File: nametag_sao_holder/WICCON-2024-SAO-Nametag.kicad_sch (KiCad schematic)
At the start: 20 parts, among them J1 Conn_02x03_Odd_Even, J2 Conn_02x03_Odd_Even, J3 Conn_02x03_Odd_Even, J4 Conn_02x03_Odd_Even, J5 Conn_02x03_Odd_Even, J6 Conn_02x03_Odd_Even, J7 Conn_02x03_Odd_Even, J8 Conn_02x03_Odd_Even, SW1 ON/OFF, U1 QX2303L33E

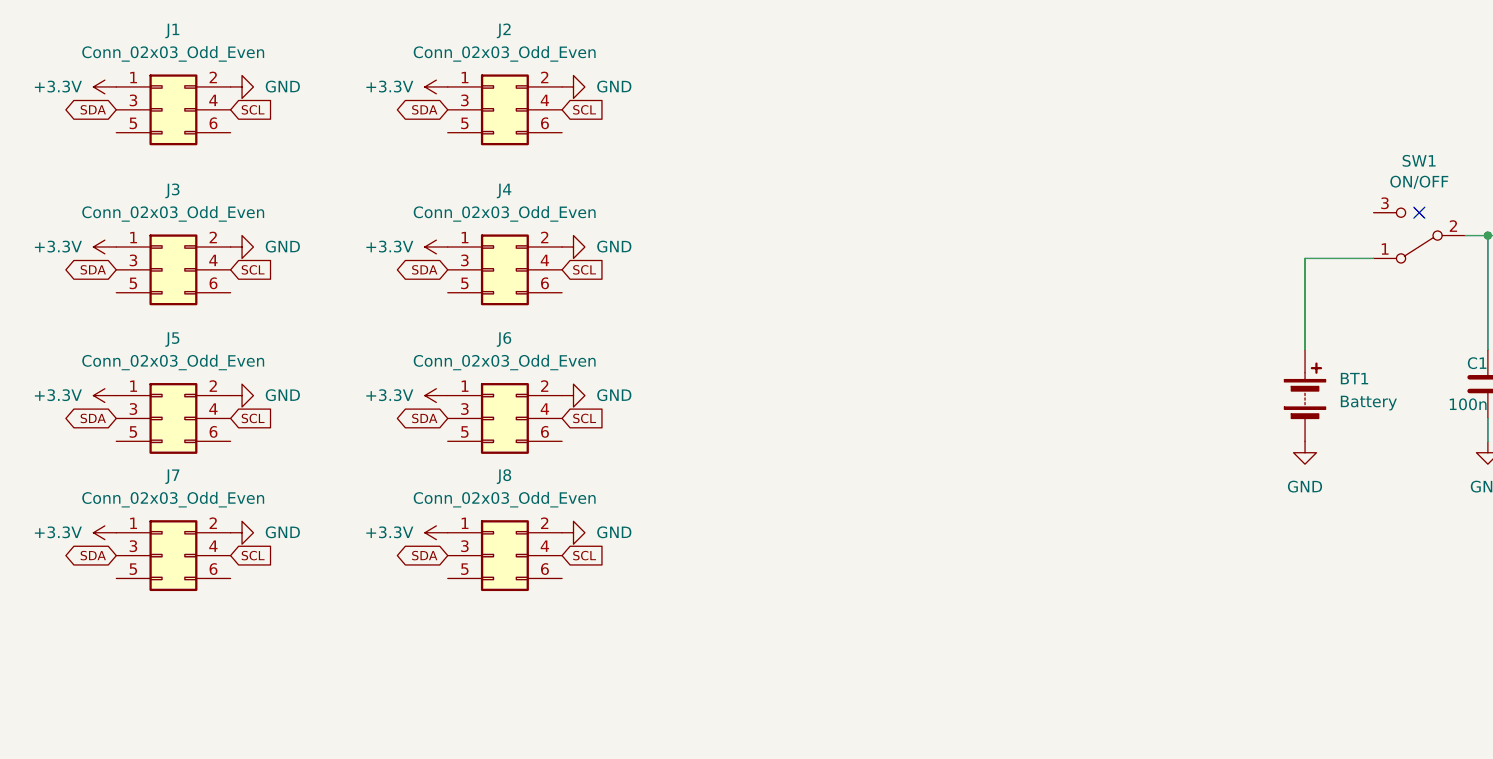
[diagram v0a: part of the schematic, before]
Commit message: Apply some improvements based on review by Paul
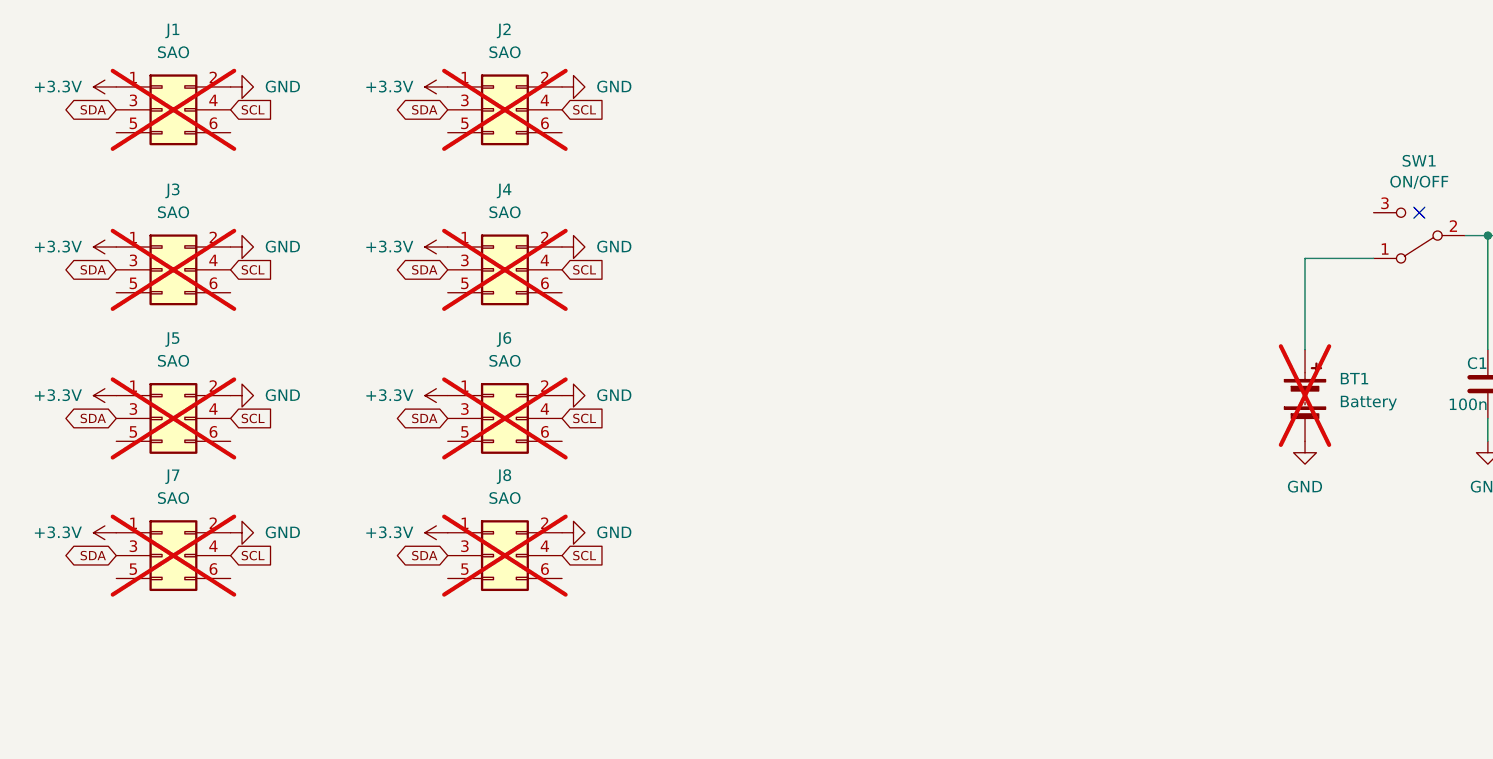
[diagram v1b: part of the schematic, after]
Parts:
- BT1: now not fitted; now left out of the parts list
- C1, C3: LCSC (none) -> C361203
- D1: LCSC (none) -> C5185907
- J1, J2, J3, J4, J5, J6, J7, J8: value Conn_02x03_Odd_Even -> SAO; now not fitted; now left out of the parts list
- SW1: LCSC (none) -> C319020
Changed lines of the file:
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@@
 			)
 		)
-		(property "Datasheet" "http://www.vishay.com/docs/88525/1n5817.pdf"
+		(property "Datasheet" "https://www.lcsc.com/product-detail/Schottky-Diodes_Slkor-SLKORMICRO-Elec-1N5819W_C5185907.html"
 			(at 222.25 44.45 0)
 			(effects
@@
 			)
 		)
+		(property "LCSC" "C5185907"
+			(at 222.25 44.45 0)
+			(effects
+				(font
+					(size 1.27 1.27)
+				)
+				(hide yes)
+			)
+		)
 		(pin "1"
 		)
@@
 			)
 		)
-		(property "Datasheet" ""
+		(property "Datasheet" "https://www.lcsc.com/product-detail/Power-Inductors_COILANK-INTERNATIONAL-ABG06A28M470_C253589.html"
 			(at 204.47 44.45 0)
 			(effects
@@
 			)
 		)
-		(property "Datasheet" "~"
+		(property "Datasheet" "https://www.lcsc.com/product-detail/Multilayer-Ceramic-Capacitors-MLCC-SMD-SMT_TDK-C1005X5R1E104KT000E_C361203.html"
 			(at 193.04 60.96 0)
 			(effects
@@
 		)
 		(property "Description" ""
+			(at 193.04 60.96 0)
+			(effects
+				(font
+					(size 1.27 1.27)
+				)
+				(hide yes)
+			)
+		)
+		(property "LCSC" "C361203"
 			(at 193.04 60.96 0)
 			(effects
@@
 			)
 		)
-		(property "Datasheet" "~"
+		(property "Datasheet" "https://www.lcsc.com/product-detail/Slide-Switches_XKB-Connection-SK-3296S-01-L1_C319020.html"
 			(at 185.42 44.45 0)
 			(effects
@@
 			)
 		)
+		(property "LCSC" "C319020"
+			(at 185.42 44.45 0)
+			(effects
+				(font
+					(size 1.27 1.27)
+				)
+				(hide yes)
+			)
+		)
 		(pin "1"
 		)
@@
 		(unit 1)
 		(exclude_from_sim no)
-		(in_bom yes)
-		(on_board yes)
-		(dnp no)
+		(in_bom no)
+		(on_board yes)
+		(dnp yes)
 		(fields_autoplaced yes)
 		(property "Reference" "J3"
@@
 			)
 		)
-		(property "Value" "Conn_02x03_Odd_Even"
+		(property "Value" "SAO"
 			(at 46.99 41.91 0)
 			(effects
@@
 		(unit 1)
 		(exclude_from_sim no)
-		(in_bom yes)
-		(on_board yes)
-		(dnp no)
+		(in_bom no)
+		(on_board yes)
+		(dnp yes)
 		(fields_autoplaced yes)
 		(property "Reference" "J7"
@@
 			)
 		)
-		(property "Value" "Conn_02x03_Odd_Even"
+		(property "Value" "SAO"
 			(at 46.99 73.66 0)
 			(effects
@@
 		(unit 1)
 		(exclude_from_sim no)
-		(in_bom yes)
-		(on_board yes)
-		(dnp no)
+		(in_bom no)
+		(on_board yes)
+		(dnp yes)
 		(fields_autoplaced yes)
 		(property "Reference" "J1"
@@
 			)
 		)
-		(property "Value" "Conn_02x03_Odd_Even"
+		(property "Value" "SAO"
 			(at 46.99 24.13 0)
 			(effects
@@
 			)
 		)
-		(property "Datasheet" "~"
+		(property "Datasheet" "https://www.lcsc.com/product-detail/Multilayer-Ceramic-Capacitors-MLCC-SMD-SMT_TDK-C1005X5R1E104KT000E_C361203.html"
 			(at 232.41 60.96 0)
 			(effects
@@
 			)
 		)
+		(property "LCSC" "C361203"
+			(at 232.41 60.96 0)
+			(effects
+				(font
+					(size 1.27 1.27)
+				)
+				(hide yes)
+			)
+		)
 		(pin "1"
 		)
@@
 		(unit 1)
 		(exclude_from_sim no)
-		(in_bom yes)
-		(on_board yes)
-		(dnp no)
+		(in_bom no)
+		(on_board yes)
+		(dnp yes)
 		(fields_autoplaced yes)
 		(property "Reference" "J5"
@@
 			)
 		)
-		(property "Value" "Conn_02x03_Odd_Even"
+		(property "Value" "SAO"
 			(at 46.99 58.42 0)
 			(effects
@@
 		(unit 1)
 		(exclude_from_sim no)
-		(in_bom yes)
-		(on_board yes)
-		(dnp no)
+		(in_bom no)
+		(on_board yes)
+		(dnp yes)
 		(fields_autoplaced yes)
 		(property "Reference" "J8"
@@
 			)
 		)
-		(property "Value" "Conn_02x03_Odd_Even"
+		(property "Value" "SAO"
 			(at 83.82 73.66 0)
 			(effects
@@
 		(unit 1)
 		(exclude_from_sim no)
-		(in_bom yes)
-		(on_board yes)
-		(dnp no)
+		(in_bom no)
+		(on_board yes)
+		(dnp yes)
 		(fields_autoplaced yes)
 		(property "Reference" "J4"
@@
 			)
 		)
-		(property "Value" "Conn_02x03_Odd_Even"
+		(property "Value" "SAO"
 			(at 83.82 41.91 0)
 			(effects
@@
 		(unit 1)
 		(exclude_from_sim no)
-		(in_bom yes)
-		(on_board yes)
-		(dnp no)
+		(in_bom no)
+		(on_board yes)
+		(dnp yes)
 		(fields_autoplaced yes)
 		(property "Reference" "J2"
@@
 			)
 		)
-		(property "Value" "Conn_02x03_Odd_Even"
+		(property "Value" "SAO"
 			(at 83.82 24.13 0)
 			(effects
@@
 		(unit 1)
 		(exclude_from_sim no)
-		(in_bom yes)
-		(on_board yes)
-		(dnp no)
+		(in_bom no)
+		(on_board yes)
+		(dnp yes)
 		(fields_autoplaced yes)
 		(property "Reference" "BT1"
@@
 		(unit 1)
 		(exclude_from_sim no)
-		(in_bom yes)
-		(on_board yes)
-		(dnp no)
+		(in_bom no)
+		(on_board yes)
+		(dnp yes)
 		(fields_autoplaced yes)
 		(property "Reference" "J6"
@@
 			)
 		)
-		(property "Value" "Conn_02x03_Odd_Even"
+		(property "Value" "SAO"
 			(at 83.82 58.42 0)
 			(effects

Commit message: Add missing production files
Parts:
- H1, H2: LCSC (none) -> -
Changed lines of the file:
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@@
+			)
+		)
+		(property "LCSC" "-"
+			(at 250.19 158.75 0)
+			(effects
+				(font
+					(size 1.27 1.27)
+				)
+				(hide yes)
 			)
 		)
@@
 			(at 250.19 153.67 0)
 			(effects
+				(font
+					(size 1.27 1.27)
+				)
+				(hide yes)
+			)
+		)
+		(property "LCSC" "-"
+			(at 250.19 153.67 0)
+			(effects

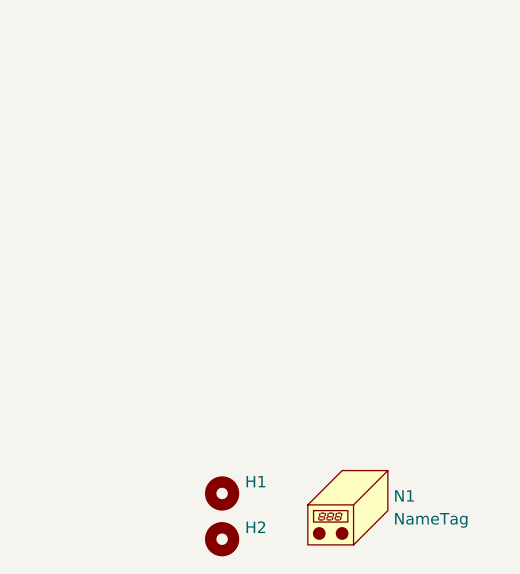
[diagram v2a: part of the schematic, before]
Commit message: Added text and art
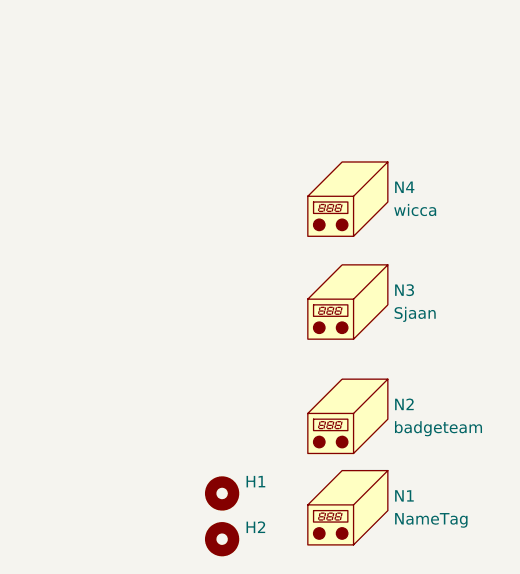
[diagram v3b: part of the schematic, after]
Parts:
- added N2: badgeteam, Library:stamp, symbol Mechanical:Housing
- added N3: Sjaan, Library:Chantal, symbol Mechanical:Housing
- added N4: wicca, Library:full_wicca_logo, symbol Mechanical:Housing
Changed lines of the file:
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@@
+	)
+	(symbol
+		(lib_id "Mechanical:Housing")
+		(at 265.43 132.08 0)
+		(unit 1)
+		(exclude_from_sim yes)
+		(in_bom no)
+		(on_board yes)
+		(dnp no)
+		(fields_autoplaced yes)
+		(property "Reference" "N3"
+			(at 269.24 131.1274 0)
+			(effects
+				(font
+					(size 1.27 1.27)
+				)
+				(justify left)
+			)
+		)
+		(property "Value" "Sjaan"
+			(at 269.24 133.6674 0)
+			(effects
+				(font
+					(size 1.27 1.27)
+				)
+				(justify left)
+			)
+		)
+		(property "Footprint" "Library:Chantal"
+			(at 266.7 130.81 0)
+			(effects
+				(font
+					(size 1.27 1.27)
+				)
+				(hide yes)
+			)
+		)
+		(property "Datasheet" ""
+			(at 266.7 130.81 0)
+			(effects
+				(font
+					(size 1.27 1.27)
+				)
+				(hide yes)
+			)
+		)
+		(property "Description" "Housing"
+			(at 265.43 132.08 0)
+			(effects
+				(font
+					(size 1.27 1.27)
+				)
+				(hide yes)
+			)
+		)
+		(property "LCSC" "-"
+			(at 265.43 132.08 0)
+			(effects
+				(font
+					(size 1.27 1.27)
+				)
+				(hide yes)
+			)
+		)
+		(instances
+			(project "WICCON-2024-SAO-Nametag"
+				(path "/f3abeae8-06bc-456b-81bc-945955c4341d"
+					(reference "N3")
+					(unit 1)
+				)
+			)
+		)
 	)
 	(symbol
@@
 	)
 	(symbol
+		(lib_id "Mechanical:Housing")
+		(at 265.43 144.78 0)
+		(unit 1)
+		(exclude_from_sim yes)
+		(in_bom no)
+		(on_board yes)
+		(dnp no)
+		(fields_autoplaced yes)
+		(property "Reference" "N2"
+			(at 269.24 143.8274 0)
+			(effects
+				(font
+					(size 1.27 1.27)
+				)
+				(justify left)
+			)
+		)
+		(property "Value" "badgeteam"
+			(at 269.24 146.3674 0)
+			(effects
+				(font
+					(size 1.27 1.27)
+				)
+				(justify left)
+			)
+		)
+		(property "Footprint" "Library:stamp"
+			(at 266.7 143.51 0)
+			(effects
+				(font
+					(size 1.27 1.27)
+				)
+				(hide yes)
+			)
+		)
+		(property "Datasheet" ""
+			(at 266.7 143.51 0)
+			(effects
+				(font
+					(size 1.27 1.27)
+				)
+				(hide yes)
+			)
+		)
+		(property "Description" "Housing"
+			(at 265.43 144.78 0)
+			(effects
+				(font
+					(size 1.27 1.27)
+				)
+				(hide yes)
+			)
+		)
+		(property "LCSC" "-"
+			(at 265.43 144.78 0)
+			(effects
+				(font
+					(size 1.27 1.27)
+				)
+				(hide yes)
+			)
+		)
+		(instances
+			(project "WICCON-2024-SAO-Nametag"
+				(path "/f3abeae8-06bc-456b-81bc-945955c4341d"
+					(reference "N2")
+					(unit 1)
+				)
+			)
+		)
+	)
+	(symbol
 		(lib_id "hh2020v1-rescue:1N5819-Diode")
 		(at 222.25 44.45 180)
@@
 		)
 		(instances
-			(project ""
+			(project "WICCON-2024-SAO-Nametag"
 				(path "/f3abeae8-06bc-456b-81bc-945955c4341d"
 					(reference "H1")
 					(unit 1)
 				)
+			)
+		)
+	)
+	(symbol
+		(lib_id "Mechanical:Housing")
+		(at 265.43 120.65 0)
+		(unit 1)
+		(exclude_from_sim yes)
+		(in_bom no)
+		(on_board yes)
+		(dnp no)
+		(fields_autoplaced yes)
+		(property "Reference" "N4"
+			(at 269.24 119.6974 0)
+			(effects
+				(font
+					(size 1.27 1.27)
+				)
+				(justify left)
+			)
+		)
+		(property "Value" "wicca"
+			(at 269.24 122.2374 0)
+			(effects
+				(font
+					(size 1.27 1.27)
+				)
+				(justify left)
+			)
+		)
+		(property "Footprint" "Library:full_wicca_logo"
+			(at 266.7 119.38 0)
+			(effects
+				(font
+					(size 1.27 1.27)
+				)
+				(hide yes)
+			)
+		)
+		(property "Datasheet" ""
+			(at 266.7 119.38 0)
+			(effects
+				(font
+					(size 1.27 1.27)
+				)
+				(hide yes)
+			)
+		)
+		(property "Description" "Housing"
+			(at 265.43 120.65 0)
+			(effects
+				(font
+					(size 1.27 1.27)
+				)
+				(hide yes)
+			)
+		)
+		(property "LCSC" "-"
+			(at 265.43 120.65 0)
+			(effects
+				(font
+					(size 1.27 1.27)
+				)
+				(hide yes)
+			)
+		)
+		(instances
+			(project "WICCON-2024-SAO-Nametag"
+				(path "/f3abeae8-06bc-456b-81bc-945955c4341d"
+					(reference "N4")
+					(unit 1)
+				)

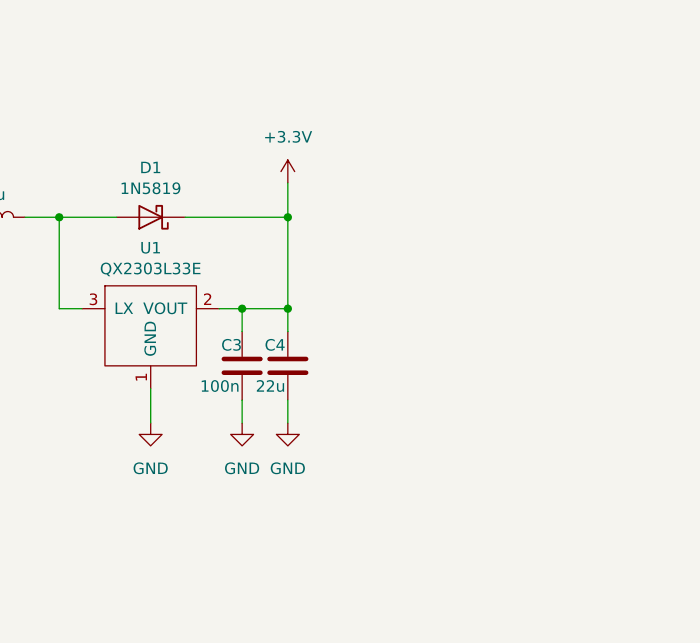
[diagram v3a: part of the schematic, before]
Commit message: Small fixes, change inductor, add power LED
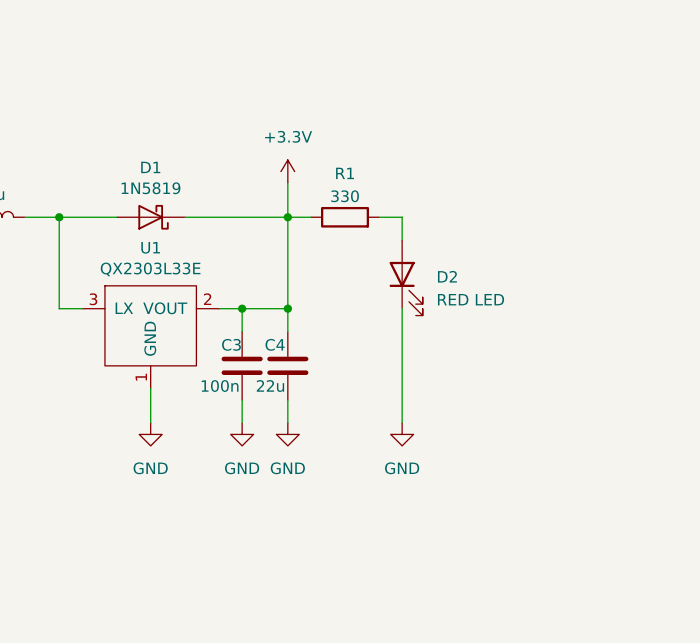
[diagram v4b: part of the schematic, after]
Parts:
- added D2: RED LED, LED_SMD:LED_0603_1608Metric, symbol SparkFun-LED:LED
- added R1: 330, Resistor_SMD:R_0402_1005Metric, symbol Device:R
- L1: footprint Inductor_SMD:L_Cenker_CKCS6020 -> Library:IND-SMD_L5.0-W5.0; LCSC C253589 -> C520357
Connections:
- net +3.3V: now also R1.1
- net GND: now also D2.1 (K)
- new net: D2.2 (A), R1.2
